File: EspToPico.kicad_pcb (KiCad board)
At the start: 2 copper layers, 25.8 x 83.7 mm, 11 parts, among them J1 Conn_01x20_Pin, J2 Conn_01x20_Pin, J3 USB_C_Receptacle_USB2.0_16P, U2 AP2112K-3.3, U3 TPD3E001DRLR, U4 ESP32-S3-WROOM-1

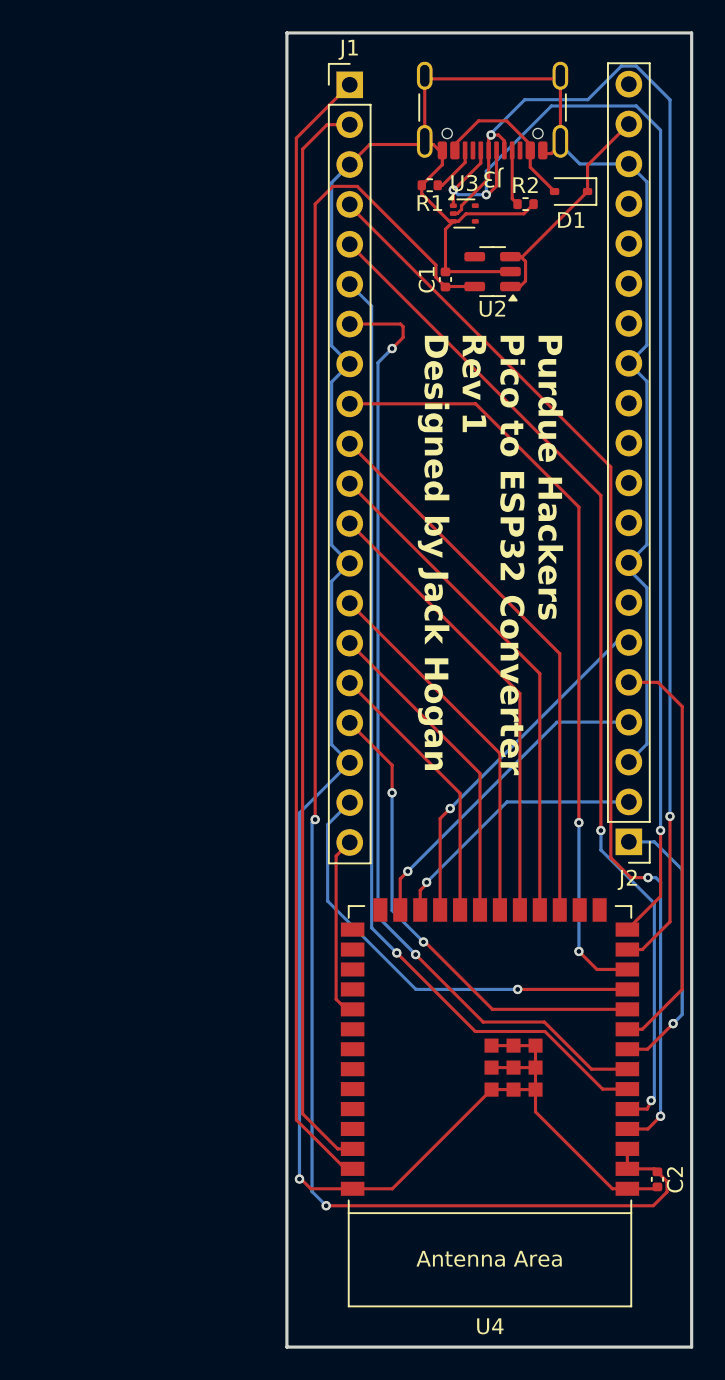
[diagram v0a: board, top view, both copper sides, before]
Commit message: Added capacitors to the voltage regulator, added through-hole to the ESP32 for hand-soldering, and updated some routing.
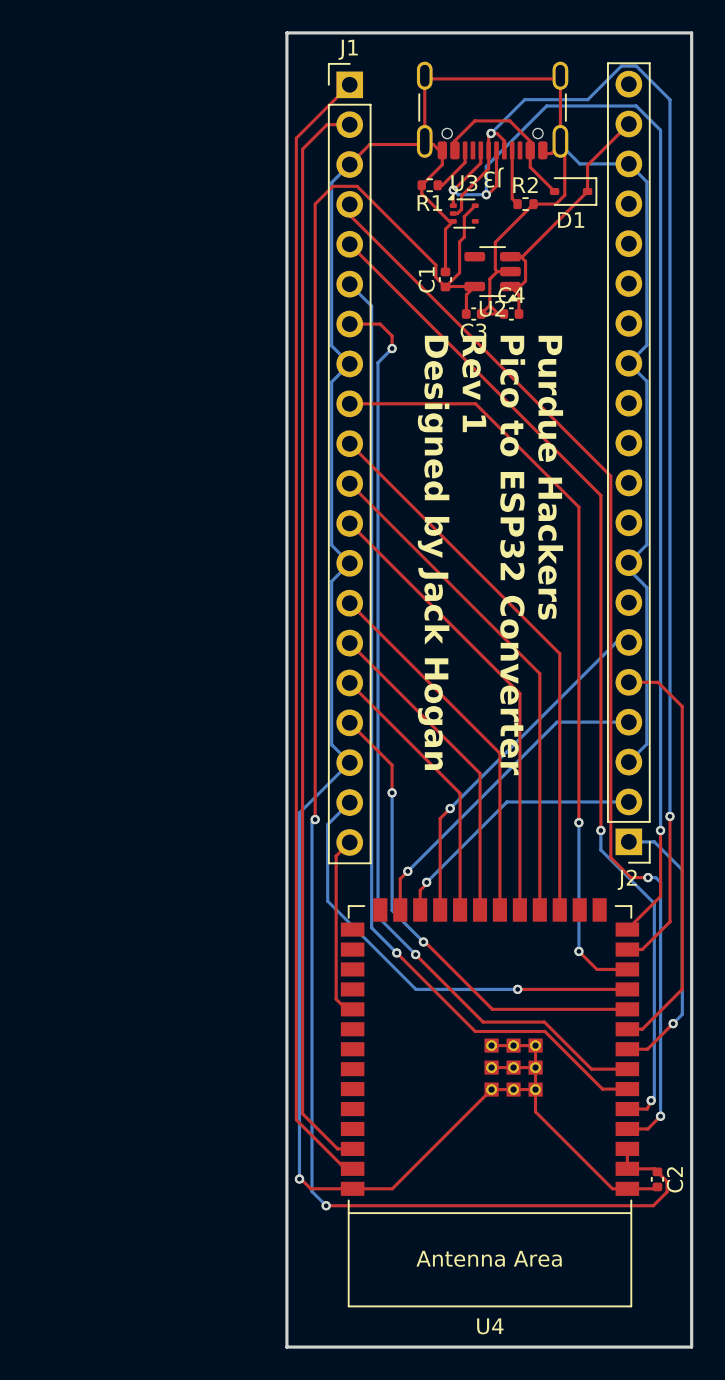
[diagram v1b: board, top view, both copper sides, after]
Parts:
- added C3: 1uF, Capacitor_SMD:C_0402_1005Metric, F.Cu at (97.9, 44.6)
- added C4: 1uF, Capacitor_SMD:C_0402_1005Metric, F.Cu at (100.3, 44.6)
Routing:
- net GND: track 196.2 -> 204.2 mm
- net +3V3: track 105.1 -> 113.1 mm
- net +5V: track 15.5 -> 17.4 mm
- net LED_BOTTOM_LEFT_B_SIG: track 61.7 -> 60.4 mm
- net Net-(D1-A): track 10.3 -> 11.3 mm

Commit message: Started conversion to ESP32
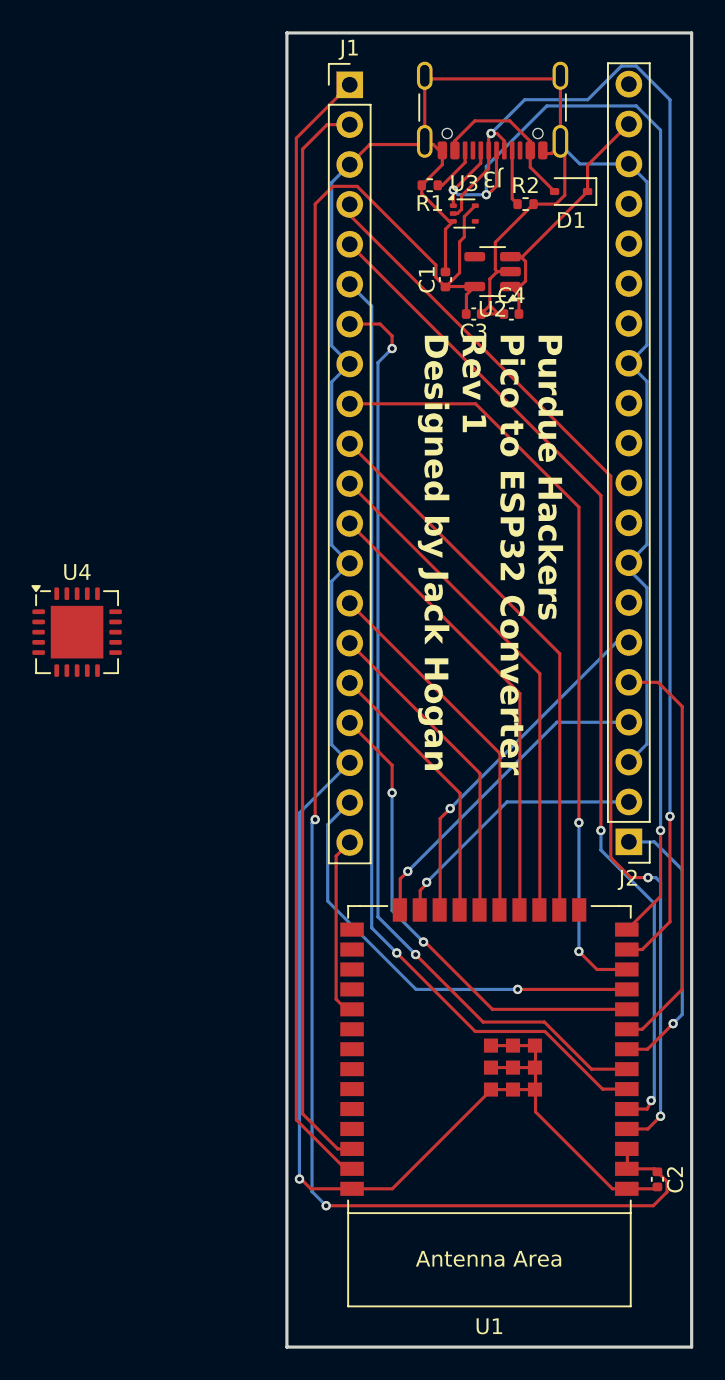
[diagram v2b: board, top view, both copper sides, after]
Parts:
- added U1: ESP32-WROOM-E, PCM_Espressif:ESP32-WROOM-32E, F.Cu at (98.9, 93.3)
- U4: value ESP32-S3-WROOM-1 -> MCP2200-I-MQ; footprint PCM_Espressif:ESP32-S3-WROOM-1 -> Package_DFN_QFN:QFN-20-1EP_5x5mm_P0.65mm_EP3.35x3.35mm
- moved U4 37.8 mm to (72.6, 64.9), turned to 0 degrees
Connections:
- U4 pad 1: GND -> +3V3
- U4 pad 10: LED_TOP_G_SIG -> unconnected-(U4-CTS-Pad10)
- U4 pad 11: LED_TOP_B_SIG -> unconnected-(U4-GP2-Pad11)
- U4 pad 12: LED_BOTTOM_RIGHT_R_SIG -> unconnected-(U4-GP1/USB-CFG-Pad12)
- U4 pad 13: JTAG_D- -> unconnected-(U4-GP0/SSPND-Pad13)
- U4 pad 14: JTAG_D+ -> +3V3
- U4 pad 15: unconnected-(U4-GPIO3/TOUCH3/ADC1_CH2-Pad15) -> JTAG_D-
- U4 pad 16: unconnected-(U4-GPIO46-Pad16) -> JTAG_D+
- U4 pad 17: LED_BOTTOM_RIGHT_G_SIG -> GND
- U4 pad 18: LED_BOTTOM_RIGHT_B_SIG -> +3V3
- U4 pad 19: LED_RIGHT_R_SIG -> unconnected-(U4-OSC1-Pad19)
- U4 pad 2: +3V3 -> unconnected-(U4-GP7/TxLED-Pad2)
- U4 pad 20: LED_RIGHT_G_SIG -> unconnected-(U4-OSC2-Pad20)
- U4 pad 21: LED_RIGHT_B_SIG -> unconnected-(U4-EP-Pad21)
- U4 pad 3: +3V3 -> unconnected-(U4-GP6/RxLED-Pad3)
- U4 pad 4: LED_CENTER_B_SIG -> unconnected-(U4-GP5-Pad4)
- U4 pad 5: LED_BOTTOM_LEFT_R_SIG -> unconnected-(U4-GP4-Pad5)
- U4 pad 6: LED_BOTTOM_LEFT_G_SIG -> unconnected-(U4-GP3-Pad6)
- U4 pad 7: LED_BOTTOM_LEFT_B_SIG -> ESP_RX
- U4 pad 8: EEPROM_MISO -> unconnected-(U4-RTS-Pad8)
- U4 pad 9: EEPROM_MOSI -> ESP_TX

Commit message: Updated to ESP32
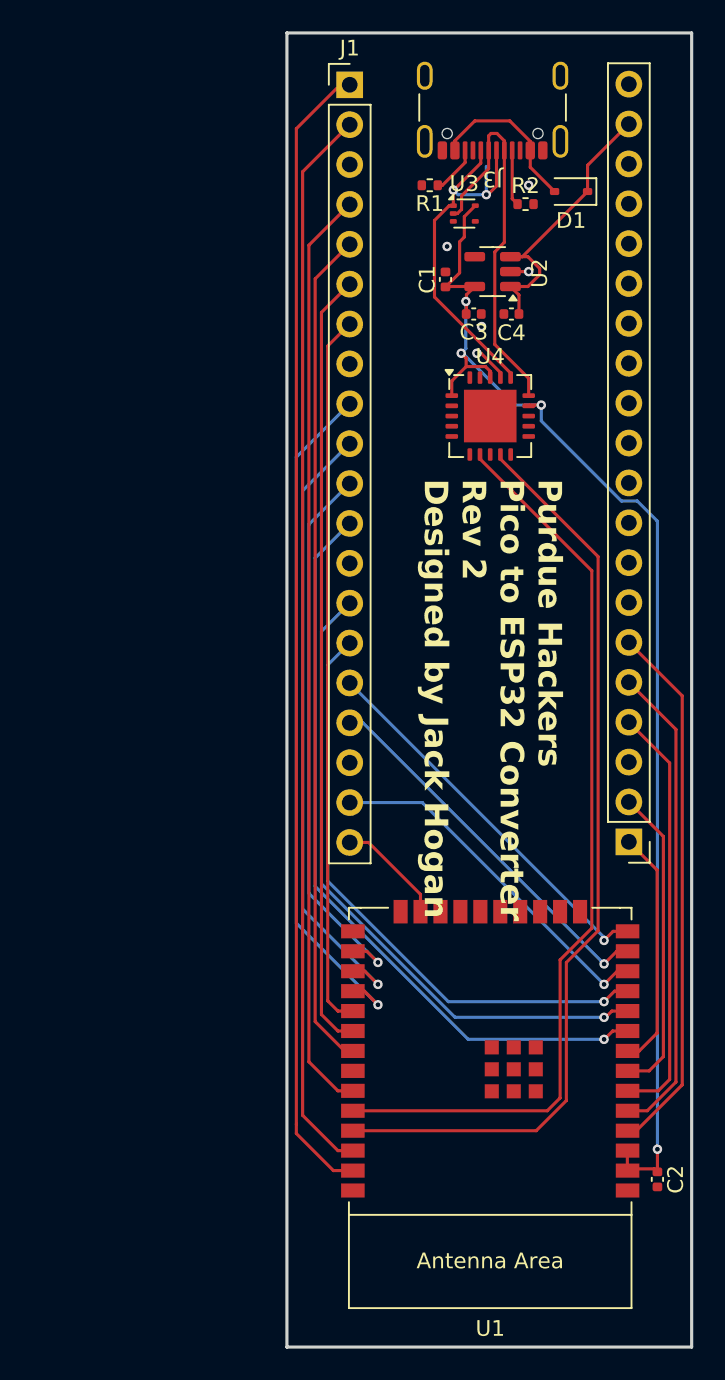
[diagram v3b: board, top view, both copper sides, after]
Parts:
- moved U4 29.7 mm to (99.0, 51.1)
- moved U1 0.12 mm to (99.0, 93.4)
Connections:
- U1 pad 10: unconnected-(U1-DAC_1/ADC2_CH8/GPIO25-Pad10) -> LED_RIGHT_G_SIG
- U1 pad 11: unconnected-(U1-DAC_2/ADC2_CH9/GPIO26-Pad11) -> LED_RIGHT_B_SIG
- U1 pad 12: unconnected-(U1-ADC2_CH7/GPIO27-Pad12) -> LED_TOP_B_SIG
- U1 pad 13: unconnected-(U1-MTMS/GPIO14/ADC2_CH6-Pad13) -> LED_TOP_G_SIG
- U1 pad 14: unconnected-(U1-MTDI/GPIO12/ADC2_CH5-Pad14) -> LED_TOP_R_SIG
- U1 pad 23: unconnected-(U1-MTDO/GPIO15/ADC2_CH3-Pad23) -> BUTTON_SWITCH
- U1 pad 26: unconnected-(U1-ADC2_CH0/GPIO4-Pad26) -> LED_BOTTOM_RIGHT_B_SIG
- U1 pad 27: unconnected-(U1-GPIO16-Pad27) -> LED_BOTTOM_RIGHT_G_SIG
- U1 pad 28: unconnected-(U1-GPIO17-Pad28) -> LED_BOTTOM_RIGHT_R_SIG
- U1 pad 29: unconnected-(U1-GPIO5-Pad29) -> LED_BOTTOM_LEFT_B_SIG
- U1 pad 30: unconnected-(U1-GPIO18-Pad30) -> LED_BOTTOM_LEFT_G_SIG
- U1 pad 31: unconnected-(U1-GPIO19-Pad31) -> LED_BOTTOM_LEFT_R_SIG
- U1 pad 33: unconnected-(U1-GPIO21-Pad33) -> LED_CENTER_B_SIG
- U1 pad 36: unconnected-(U1-GPIO22-Pad36) -> LED_CENTER_G_SIG
- U1 pad 37: unconnected-(U1-GPIO23-Pad37) -> LED_CENTER_R_SIG
- U1 pad 4: unconnected-(U1-SENSOR_VP/GPIO36/ADC1_CH0-Pad4) -> BUTTON_LED
- U1 pad 5: unconnected-(U1-SENSOR_VN/GPIO39/ADC1_CH3-Pad5) -> EEPROM_MOSI
- U1 pad 6: unconnected-(U1-GPIO34/ADC1_CH6-Pad6) -> EEPROM_SCK
- U1 pad 7: unconnected-(U1-GPIO35/ADC1_CH7-Pad7) -> EEPROM_CS
- U1 pad 8: unconnected-(U1-32K_XP/GPIO32/ADC1_CH4-Pad8) -> EEPROM_MISO
- U1 pad 9: unconnected-(U1-32K_XN/GPIO33/ADC1_CH5-Pad9) -> LED_RIGHT_R_SIG
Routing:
- net GND: track 204.2 -> 4.10 mm, vias 1 -> 5
- net ESP_TX: track 0.00 -> 59.0 mm
- net ESP_RX: track 0.00 -> 58.3 mm
- net JTAG_D-: track 77.9 -> 24.7 mm, vias 2 -> 0
- net JTAG_D+: track 76.4 -> 24.9 mm, vias 3 -> 2
- net +3V3: track 113.1 -> 81.8 mm, vias 2 -> 4
- net LED_RIGHT_R_SIG: track 29.1 -> 48.3 mm, vias 0 -> 1
- net LED_RIGHT_G_SIG: track 23.5 -> 42.0 mm, vias 0 -> 1
- net LED_RIGHT_B_SIG: track 20.4 -> 38.4 mm, vias 0 -> 1
- net LED_BOTTOM_LEFT_B_SIG: track 60.4 -> 45.6 mm, vias 2 -> 0
- net LED_BOTTOM_LEFT_G_SIG: track 62.1 -> 49.7 mm, vias 1 -> 0
- net BUTTON_LED: track 22.6 -> 34.3 mm, vias 1 -> 0
- net LED_BOTTOM_LEFT_R_SIG: track 64.8 -> 53.6 mm, vias 2 -> 0
- net LED_CENTER_B_SIG: track 69.9 -> 59.9 mm, vias 2 -> 0
- net LED_TOP_R_SIG: track 17.4 -> 24.9 mm, vias 0 -> 1
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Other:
- board text added: "Purdue Hackers Pico to ESP32 Converter Rev 2 Designed by Jack Hogan"
- board text removed: "Purdue Hackers Pico to ESP32 Converter Rev 1 Designed by Jack Hogan"

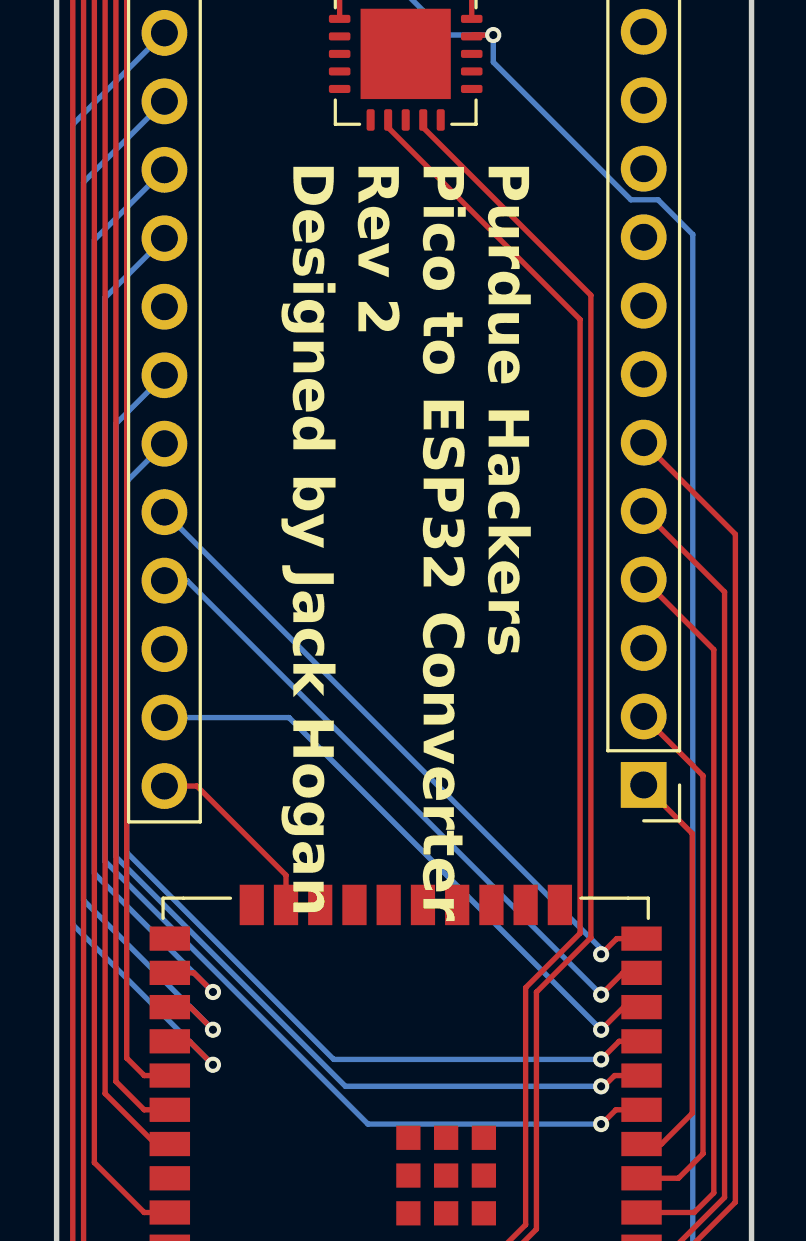
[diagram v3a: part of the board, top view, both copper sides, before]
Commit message: Fixed silkscreen
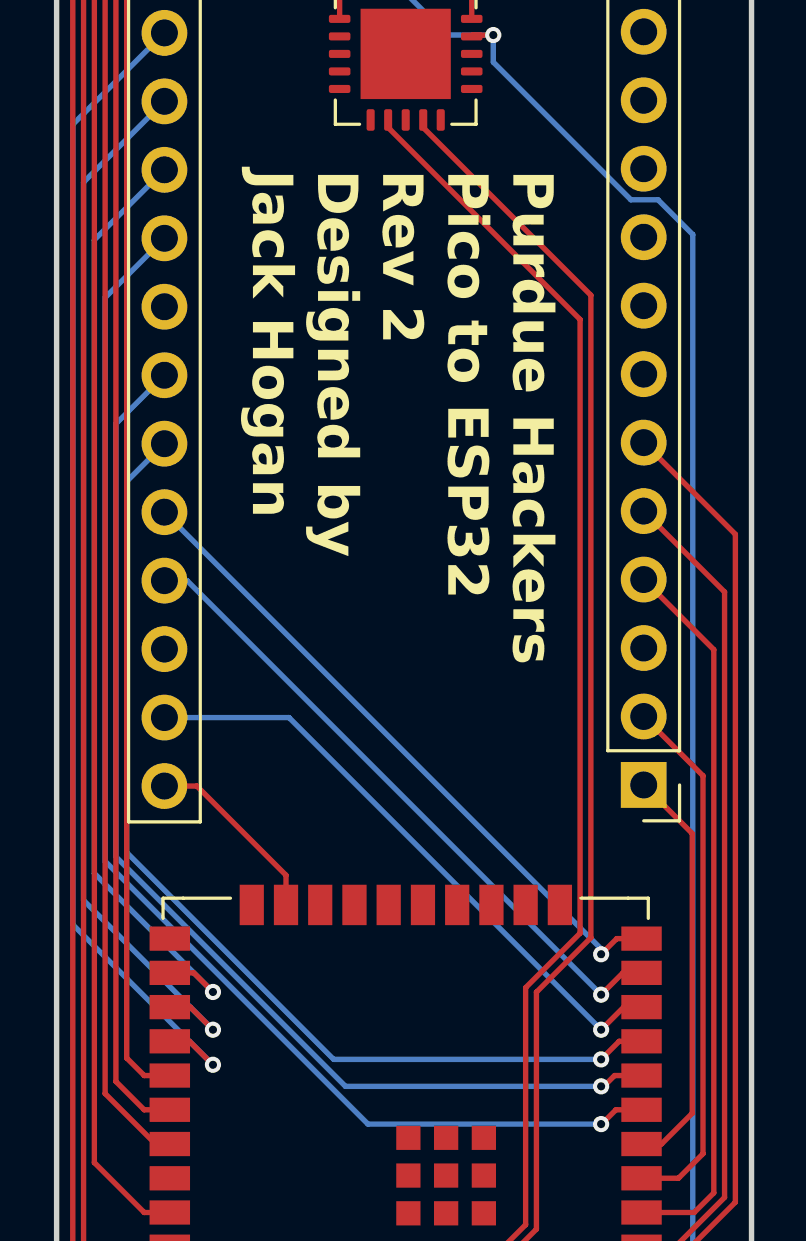
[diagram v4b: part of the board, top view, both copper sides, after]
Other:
- board text added: "Purdue Hackers Pico to ESP32 Rev 2 Designed by Jack Hogan"
- board text removed: "Purdue Hackers Pico to ESP32 Converter Rev 2 Designed by Jack Hogan"
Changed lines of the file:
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@@
 		(layer "Edge.Cuts")
 	)
-	(gr_text "Purdue Hackers\nPico to ESP32 Converter\nRev 2\nDesigned by Jack Hogan"
-		(at 94.6 55.1 270)
+	(gr_text "Purdue Hackers\nPico to ESP32\nRev 2\nDesigned by\nJack Hogan"
+		(at 93.1 55.4 270)
 		(layer "F.SilkS")
 		(effects

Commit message: Electrical and Routing fixes
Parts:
- added Y1: CSTCE12M0G15L, footprints:CSTCE12M0G15L, F.Cu at (94.7, 46.4)
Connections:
- U4 pad 19: unconnected-(U4-OSC1-Pad19) -> Net-(U4-OSC1)
- U4 pad 20: unconnected-(U4-OSC2-Pad20) -> Net-(U4-OSC2)
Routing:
- net GND: track 4.10 -> 27.9 mm
- net +3V3: track 81.8 -> 90.9 mm, vias 4 -> 5
- net Net-(U4-OSC2): track 0.00 -> 5.74 mm
- net Net-(U4-OSC1): track 0.00 -> 3.64 mm
- net JTAG_D+: track 24.9 -> 22.2 mm, vias 2 -> 0
- net JTAG_D-: track 24.7 -> 23.2 mm
